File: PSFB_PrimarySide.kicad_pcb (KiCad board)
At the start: 4 copper layers, 112 x 74 mm, 133 parts, among them J10 PSFB_Control, J5 Supply, J6 Supply, J7 Supply, J8 Supply, Q1 C3M0065100K, Q2 C3M0065100K, Q3 C3M0065100K, Q4 C3M0065100K, U1 74LVC1G08, U2 74LVC1G08, U3 74LVC1G08, U4 74LVC1G08, U6 USBLC6-2SC6, U7 USBLC6-2SC6, U8 USBLC6-2SC6, U9 USBLC6-2SC6

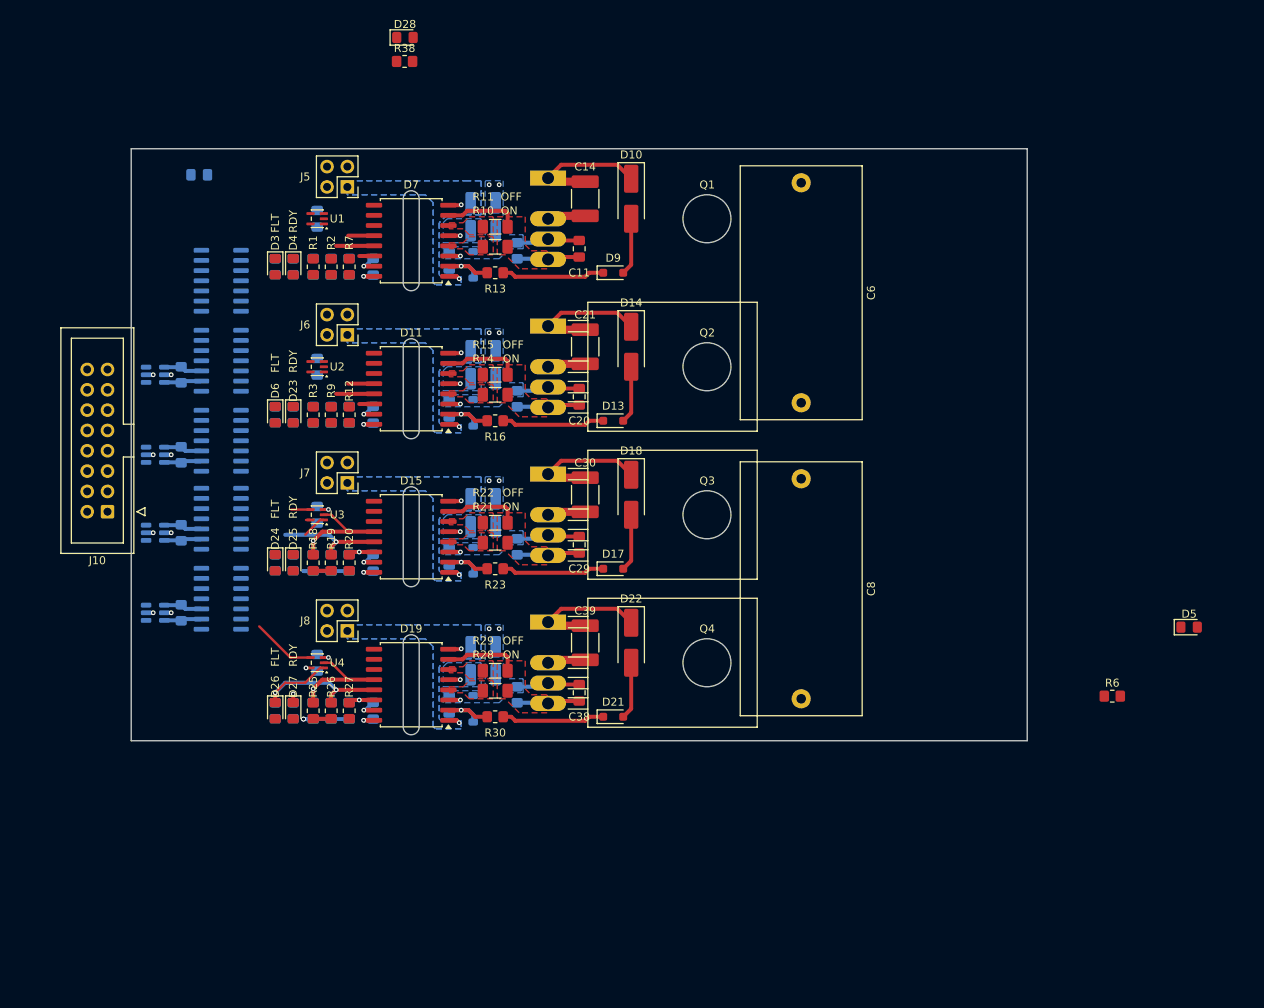
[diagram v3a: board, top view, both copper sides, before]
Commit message: VER1.0: добавил разъем под FFC
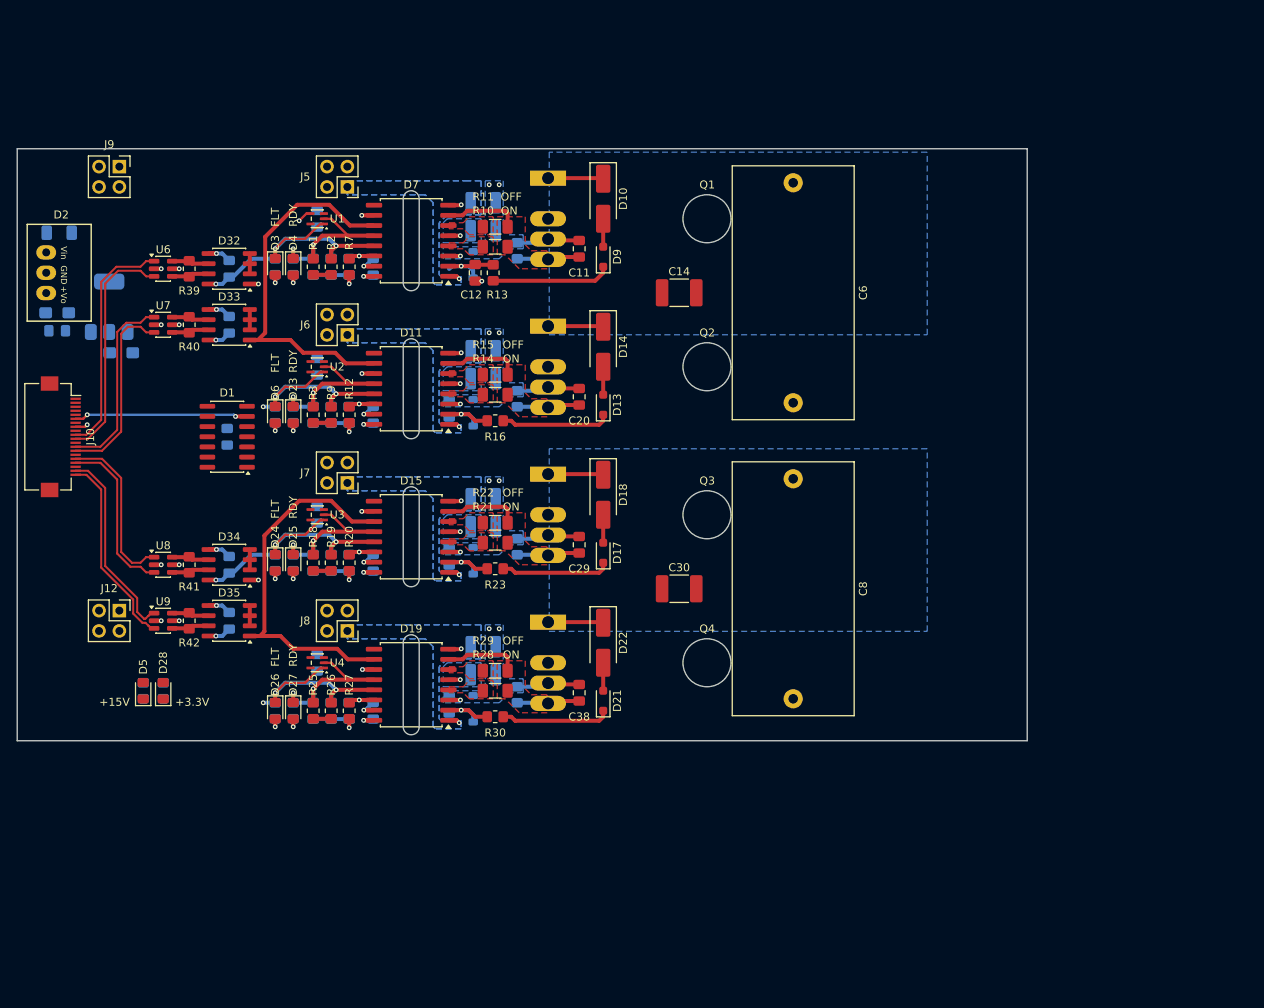
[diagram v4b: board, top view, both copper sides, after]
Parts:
- removed C21, C39: 220p, Capacitor_SMD:C_1812_4532Metric_Pad1.57x3.40mm_HandSolder
- removed D29, D30, D31: DS90LV019, Package_SO:SO-14_3.9x8.65mm_P1.27mm
- added C3: 22u, Capacitor_Tantalum_SMD:CP_EIA-3216-18_Kemet-A_HandSolder, B.Cu at (26.5, 97.5)
- added C45: 100n, Capacitor_SMD:C_0805_2012Metric_Pad1.18x1.45mm_HandSolder, B.Cu at (40.0, 87.0)
- added C46: 100n, Capacitor_SMD:C_0805_2012Metric_Pad1.18x1.45mm_HandSolder, B.Cu at (40.0, 94.0)
- added C47: 100n, Capacitor_SMD:C_0805_2012Metric_Pad1.18x1.45mm_HandSolder, B.Cu at (40.0, 124.0)
- added C48: 100n, Capacitor_SMD:C_0805_2012Metric_Pad1.18x1.45mm_HandSolder, B.Cu at (40.0, 131.0)
- added C49: 10u, Capacitor_Tantalum_SMD:CP_EIA-3216-18_Kemet-A_HandSolder, B.Cu at (18.5, 92.5)
- added C50: 10u, Capacitor_SMD:C_1206_3216Metric_Pad1.33x1.80mm_HandSolder, B.Cu at (18.8, 82.5)
- added C53: 100n, Capacitor_SMD:C_0805_2012Metric_Pad1.18x1.45mm_HandSolder, B.Cu at (18.5, 94.8)
- added D32: MS2111, Package_SO:SO-8_3.9x4.9mm_P1.27mm, F.Cu at (40.0, 87.0)
- added D33: MS2111, Package_SO:SO-8_3.9x4.9mm_P1.27mm, F.Cu at (40.0, 94.0)
- added D34: MS2111, Package_SO:SO-8_3.9x4.9mm_P1.27mm, F.Cu at (40.0, 124.0)
- added D35: MS2111, Package_SO:SO-8_3.9x4.9mm_P1.27mm, F.Cu at (40.0, 131.0)
- added J12: Supply, Connector_PinSocket_2.54mm:PinSocket_2x02_P2.54mm_Vertical, F.Cu at (26.3, 129.7)
- added J9: Supply, Connector_PinSocket_2.54mm:PinSocket_2x02_P2.54mm_Vertical, F.Cu at (26.3, 74.2)
- added U5: AMS1117-3.3, Package_TO_SOT_SMD:SOT-223-3_TabPin2, B.Cu at (25.0, 91.8)
- C12, D1, R39, R40, R41, R42, U6, U7, U8, U9: moved to F.Cu
- C14, C30: value 220p -> 100n
- D2: value DS90LV019 -> K78xx-500R3; footprint Package_SO:SO-14_3.9x8.65mm_P1.27mm -> MORNSUN:K78xx-500R3 ÕýÊä³ö; moved to F.Cu
- J10: footprint Connector_IDC:IDC-Header_2x08_P2.54mm_Vertical -> Connector_FFC-FPC:Hirose_FH12-20S-0.5SH_1x20-1MP_P0.50mm_Horizontal
- R38, R6: moved to B.Cu
- moved D5 131.0 mm to (29.2, 139.8), turned to 90 degrees
- moved R6 121.1 mm to (29.2, 139.8), turned to -90 degrees
- moved D28 87.1 mm to (31.8, 139.8), turned to 90 degrees
- moved R38 84.3 mm to (31.8, 139.8), turned to -90 degrees
- moved C44 32.9 mm to (39.8, 108.0), turned to -90 degrees
- moved D2 24.5 mm to (17.1, 87.5), turned to -90 degrees
- moved D1 19.5 mm to (39.8, 108.0)
- moved C14 16.6 mm to (96.2, 90.0), turned to 0 degrees
- moved C30 16.6 mm to (96.2, 127.0), turned to 0 degrees
- moved R40 16.3 mm to (35.0, 94.0)
- moved U7 16.3 mm to (31.8, 94.0), turned to 0 degrees
- moved R39 13.3 mm to (35.0, 87.0)
- moved U6 13.3 mm to (31.8, 87.0), turned to 0 degrees
- moved J10 11.0 mm to (18.9, 108.0), turned to -90 degrees
- moved R41 4.12 mm to (35.0, 124.0)
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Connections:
- C14 pad 2: /Driver_1/GND2 -> GNDPWR
- C15 pad 2: +5V -> +3.3V
- C24 pad 2: +5V -> +3.3V
- C30 pad 2: /Driver_3/GND2 -> GNDPWR
- C33 pad 2: +5V -> +3.3V
- C40 pad 2: +5V -> +3.3V
- C41 pad 2: +5V -> +3.3V
- C42 pad 2: +5V -> +3.3V
- C43 pad 2: +5V -> +3.3V
- C44 pad 2: +5V -> +3.3V
- C5 pad 2: +5V -> +3.3V
- D1 pad 14: +5V -> +3.3V
- D11 pad 15: +5V -> +3.3V
- D15 pad 15: +5V -> +3.3V
- D19 pad 15: +5V -> +3.3V
- D2 pad 1: GND -> +15V
- D2 pad 2: unconnected-(D2-DIN-Pad2) -> GND
- D2 pad 3: (no net) -> /+5V
- D7 pad 15: +5V -> +3.3V
- J10 pad 10: /PWM_L2_N -> /PWM_H1_P
- J10 pad 11: /ERROR -> /PWM_H1_N
- J10 pad 13: /RST -> /PWM_L1_P
- J10 pad 14: GND -> /PWM_L1_N
- J10 pad 15: +5V -> GND
- J10 pad 16: GND -> /PWM_H2_P
- J10 pad 2: GND -> +15V
- J10 pad 3: /PWM_H1_P -> GND
- J10 pad 4: /PWM_H1_N -> GND
- J10 pad 5: /PWM_L1_P -> GND
- J10 pad 6: /PWM_L1_N -> /ERROR
- J10 pad 7: /PWM_H2_P -> GND
- J10 pad 8: /PWM_H2_N -> /RST
- J10 pad 9: /PWM_L2_P -> GND
- R1 pad 2: +5V -> +3.3V
- R18 pad 2: +5V -> +3.3V
- R19 pad 2: +5V -> +3.3V
- R2 pad 2: +5V -> +3.3V
- R25 pad 2: +5V -> +3.3V
- R26 pad 2: +5V -> +3.3V
- R3 pad 2: +5V -> +3.3V
- R32 pad 2: +5V -> +3.3V
- R34 pad 2: +5V -> +3.3V
- R36 pad 2: +5V -> +3.3V
- R38 pad 2: +5V -> +3.3V
- R39 pad 1: Net-(D2-RI-) -> Net-(D32-B)
- R39 pad 2: Net-(D2-RI+) -> Net-(D32-A)
- R4 pad 2: +5V -> +3.3V
- R40 pad 1: Net-(D29-RI-) -> Net-(D33-B)
- R40 pad 2: Net-(D29-RI+) -> Net-(D33-A)
- R41 pad 1: Net-(D30-RI-) -> Net-(D34-B)
- R41 pad 2: Net-(D30-RI+) -> Net-(D34-A)
- R42 pad 1: Net-(D31-RI-) -> Net-(D35-B)
- R42 pad 2: Net-(D31-RI+) -> Net-(D35-A)
- R9 pad 2: +5V -> +3.3V
- U1 pad 5: +5V -> +3.3V
- U2 pad 5: +5V -> +3.3V
- U3 pad 5: +5V -> +3.3V
- U4 pad 5: +5V -> +3.3V
- U6 pad 1: Net-(D2-RI+) -> /PWM_H1_P
- U6 pad 3: Net-(D2-RI-) -> /PWM_H1_N
- U6 pad 4: /PWM_H1_N -> Net-(D32-B)
- U6 pad 5: +5V -> +3.3V
- U6 pad 6: /PWM_H1_P -> Net-(D32-A)
- U7 pad 1: Net-(D29-RI+) -> /PWM_L1_P
- U7 pad 3: Net-(D29-RI-) -> /PWM_L1_N
- U7 pad 4: /PWM_L1_N -> Net-(D33-B)
- U7 pad 5: +5V -> +3.3V
- U7 pad 6: /PWM_L1_P -> Net-(D33-A)
- U8 pad 1: Net-(D30-RI+) -> /PWM_H2_P
- U8 pad 3: Net-(D30-RI-) -> /PWM_H2_N
- U8 pad 4: /PWM_H2_N -> Net-(D34-B)
- U8 pad 5: +5V -> +3.3V
- U8 pad 6: /PWM_H2_P -> Net-(D34-A)
- U9 pad 1: Net-(D31-RI+) -> /PWM_L2_P
- U9 pad 3: Net-(D31-RI-) -> /PWM_L2_N
- U9 pad 4: /PWM_L2_N -> Net-(D35-B)
- U9 pad 5: +5V -> +3.3V
- U9 pad 6: /PWM_L2_P -> Net-(D35-A)
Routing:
- net +3.3V: track 0.00 -> 52.0 mm, vias 0 -> 14
- net /PWM_L1: track 0.00 -> 47.4 mm
- net /PWM_L2: track 0.00 -> 47.4 mm
- net /PWM_H1: track 0.00 -> 42.9 mm, vias 0 -> 3
- net /PWM_H2: track 0.00 -> 42.6 mm, vias 0 -> 3
- net /PWM_H1_P: track 0.00 -> 28.9 mm
- net /PWM_H1_N: track 0.00 -> 28.9 mm
- net GND: track 28.8 -> 57.7 mm, vias 13 -> 16
- net /PWM_L2_N: track 0.00 -> 24.5 mm
- net /PWM_L2_P: track 0.00 -> 24.5 mm
- net /PWM_L1_P: track 0.00 -> 23.7 mm
- net /PWM_L1_N: track 0.00 -> 23.7 mm
- net /ERROR: track 0.00 -> 21.7 mm, vias 0 -> 2
- net /PWM_H2_N: track 0.00 -> 20.9 mm
- net /PWM_H2_P: track 0.00 -> 20.9 mm
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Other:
- board size 112 x 74 mm -> 126.2 x 74 mm
- board text added: "+15V"
- board text added: "+3.3V"

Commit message: VER1.0: добавил плату питания драйверов и развел всю силовую плату
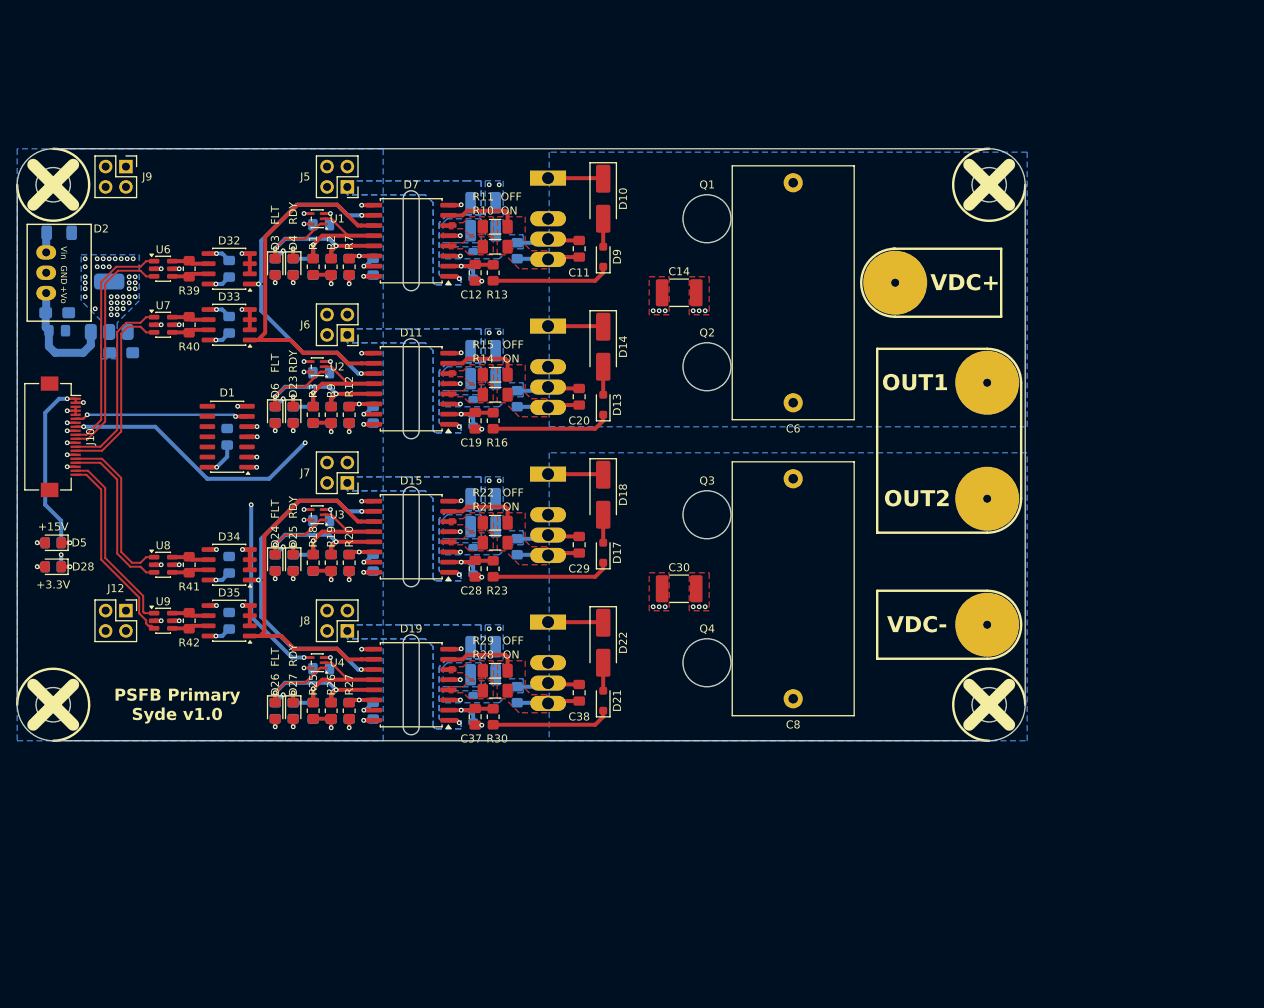
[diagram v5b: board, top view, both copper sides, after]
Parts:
- added H1: MountingHole, MountingHole:MountingHole_4.3mm_M4, F.Cu at (18.0, 76.5)
- added H2: MountingHole, MountingHole:MountingHole_4.3mm_M4, F.Cu at (18.0, 141.5)
- added H3: MountingHole, MountingHole:MountingHole_4.3mm_M4, F.Cu at (135.0, 76.5)
- added H4: MountingHole, MountingHole:MountingHole_4.3mm_M4, F.Cu at (135.0, 141.5)
- added J1: DC+, Connector_my:Bush_1x8, F.Cu at (123.2, 88.8)
- added J2: DC-, Connector_my:Bush_1x8, F.Cu at (134.8, 131.5)
- added J3: OUT1, Connector_my:Bush_1x8, F.Cu at (134.8, 101.2)
- added J4: OUT2, Connector_my:Bush_1x8, F.Cu at (134.8, 115.8)
- C19, C28, C37: moved to F.Cu
- moved D5 21.7 mm to (18.0, 121.2), turned to 180 degrees
- moved R6 21.7 mm to (18.0, 121.2), turned to 0 degrees
- moved D28 20.7 mm to (18.0, 124.2), turned to 180 degrees
- moved R38 20.7 mm to (18.0, 124.2), turned to 0 degrees
- moved C19 3.58 mm to (70.8, 106.0), turned to -90 degrees
- moved C28 3.58 mm to (70.8, 124.5), turned to -90 degrees
- moved C37 3.58 mm to (70.8, 143.0), turned to -90 degrees
- moved C40 0.90 mm to (51.5, 81.5), turned to 180 degrees
- moved C41 0.90 mm to (51.5, 100.0), turned to 180 degrees
- moved C42 0.90 mm to (51.5, 118.5), turned to 180 degrees
- moved C43 0.90 mm to (51.5, 137.0), turned to 180 degrees
- moved J12 0.82 mm to (27.1, 129.7)
- moved J9 0.82 mm to (27.1, 74.2)
- moved R16 0.25 mm to (73.0, 106.0), turned to 90 degrees
- moved R23 0.25 mm to (73.0, 124.5), turned to 90 degrees
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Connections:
- J9 pad 1: GND -> +15V
- J9 pad 3: GND -> +15V
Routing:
- net /RST: track 6.05 -> 137.0 mm, vias 5 -> 6
- net /Common_FLT1: track 1.79 -> 36.1 mm, vias 1 -> 2
- net /Common_FLT4: track 0.00 -> 29.7 mm, vias 0 -> 3
- net +15V: track 0.00 -> 25.6 mm, vias 0 -> 2
- net /Common_FLT2: track 0.00 -> 16.8 mm, vias 0 -> 2
- net /+5V: track 0.00 -> 14.5 mm
- net /Common_FLT3: track 0.00 -> 12.3 mm, vias 0 -> 2
- net +3.3V: track 52.0 -> 55.0 mm, vias 14 -> 63
- net Net-(D7-DESAT): track 9.99 -> 7.99 mm
- net /PWM_H2: track 42.6 -> 44.6 mm
- net Net-(D5-A): track 0.00 -> 1.98 mm, vias 0 -> 1
- net Net-(D28-A): track 0.00 -> 1.98 mm, vias 0 -> 1
- net GND: track 57.7 -> 59.6 mm, vias 16 -> 37
- net GNDPWR: track 17.2 -> 18.9 mm, vias 6 -> 14
- net Net-(D15-DESAT): track 9.48 -> 7.99 mm
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- added copper zone on In2.Cu, net +15V
- added copper zone on B.Cu, net +3.3V
- added copper zone on In2.Cu, net +3.3V
- added copper zone on B.Cu, net GND
- added copper zone on In1.Cu, net GND
- added copper zone on F.Cu, net GNDPWR
- added copper zone on F.Cu, net VDC
- removed copper zone on In1.Cu, net (none)
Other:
- board size 126.2 x 74 mm -> 126 x 74 mm
- board text added: "OUT1"
- board text added: "OUT2"
- board text added: "PSFB Primary Syde v1.0"
- board text added: "VDC+"
- board text added: "VDC-"

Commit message: VER1.0: добавил ресет общий
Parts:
- added Q5: ~, Package_TO_SOT_SMD:SOT-23, F.Cu at (30.2, 110.0)
- added R100: 4.7k, Resistor_SMD:R_0805_2012Metric_Pad1.20x1.40mm_HandSolder, F.Cu at (30.2, 106.8)
- added R101: 1k, Resistor_SMD:R_0805_2012Metric_Pad1.20x1.40mm_HandSolder, F.Cu at (33.2, 110.0)
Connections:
- R12 pad 1: /RST -> /Driver_1/~{RST}
- R20 pad 1: /RST -> /Driver_1/~{RST}
- R27 pad 1: /RST -> /Driver_1/~{RST}
- R7 pad 1: /RST -> /Driver_1/~{RST}
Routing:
- net /Driver_1/~{RST}: track 0.00 -> 161.1 mm, vias 0 -> 6
- net /RST: track 137.0 -> 8.45 mm, vias 6 -> 2
- net +3.3V: track 55.0 -> 60.3 mm, vias 63 -> 64
- net Net-(Q5-B): track 0.00 -> 2.33 mm
- net GND: track 59.6 -> 60.6 mm, vias 37 -> 38

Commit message: VER1.0: сделал файлы для производства
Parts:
- D1: value 74HC21 -> ~
- D11, D15, D19, D7: value NSI6651ASC-DSWR -> ~
- D2: value K78xx-500R3 -> ~
- D32, D33, D34, D35: value MS2111 -> ~
- H1, H2, H3, H4: value MountingHole -> ~
- J10: value PSFB_Control -> ~
- J12, J5, J6, J7, J8, J9: value Supply -> ~
- Q1, Q2, Q3, Q4: value C3M0065100K -> ~
- U1, U2, U3, U4: value 74LVC1G08 -> ~
- U5: value AMS1117-3.3 -> ~
- U6, U7, U8, U9: value USBLC6-2SC6 -> ~
